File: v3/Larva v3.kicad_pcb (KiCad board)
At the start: 2 copper layers, 228 x 82.1 mm, 102 parts, among them J1 Conn_02x03_Odd_Even, J2 USB_C_Receptacle_USB2.0, SW1 SW_Push, U1 ATmega32U4-M, U2 USBLC6-2SC6, Y1 Crystal_GND24_Small

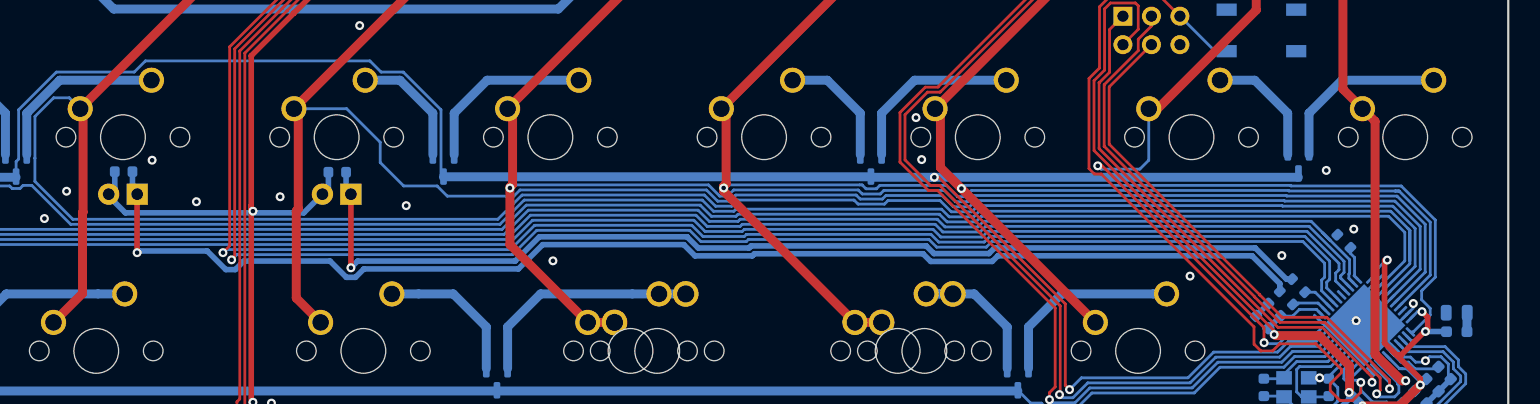
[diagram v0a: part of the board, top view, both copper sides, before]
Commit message: update LEDs
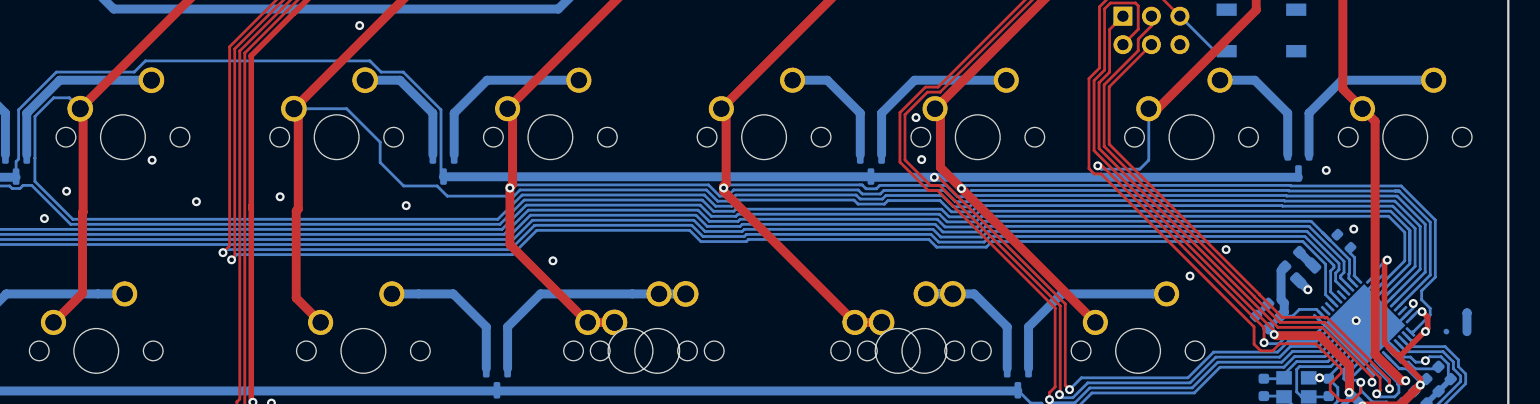
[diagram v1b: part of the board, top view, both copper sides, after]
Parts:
- removed D18: smd1, LED_SMD:LED_0603_1608Metric
- removed D23: smd2, LED_SMD:LED_0603_1608Metric
- removed R6, R9: 680, Resistor_SMD:R_0603_1608Metric
- MX27, MX28: footprint MxSwitches:MXOnly-1U -> PCM_marbastlib-mx:SW_MX_1u
- moved R14 16.0 mm to (246.6, 111.2), turned to 45 degrees
- moved D24 13.9 mm to (247.8, 112.5), turned to 45 degrees
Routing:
- net /LED2: track 114.8 -> 0.00 mm, vias 1 -> 0
- net /LED3: track 95.9 -> 0.00 mm, vias 1 -> 0
- net +5V: track 341.5 -> 319.3 mm, vias 11 -> 10
- net /LED_LEFT: track 3.26 -> 0.00 mm
- net /LED_RIGHT: track 2.73 -> 0.00 mm
- net Net-(D24-A): track 1.70 -> 3.41 mm
- net GND: track 43.5 -> 44.7 mm, vias 31 -> 32
